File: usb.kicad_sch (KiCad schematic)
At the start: 69 parts, among them J13 USB-C_GCT_USB4105-GF-A, J3 USB-C_GCT_USB4105-GF-A, Q1 SSM3J332R, Q2 BC817-25W, Q3 BCM857BS-7-F, Q4 SSM3J332R, Q5 BCM857BS-7-F, U11 AP22652W6, U15 AP22652W6, U2 TPD4E05U06QDQARQ1, U4 AP62301_TSOT, U5 TPD4E05U06QDQARQ1, U8 AP62301_TSOT

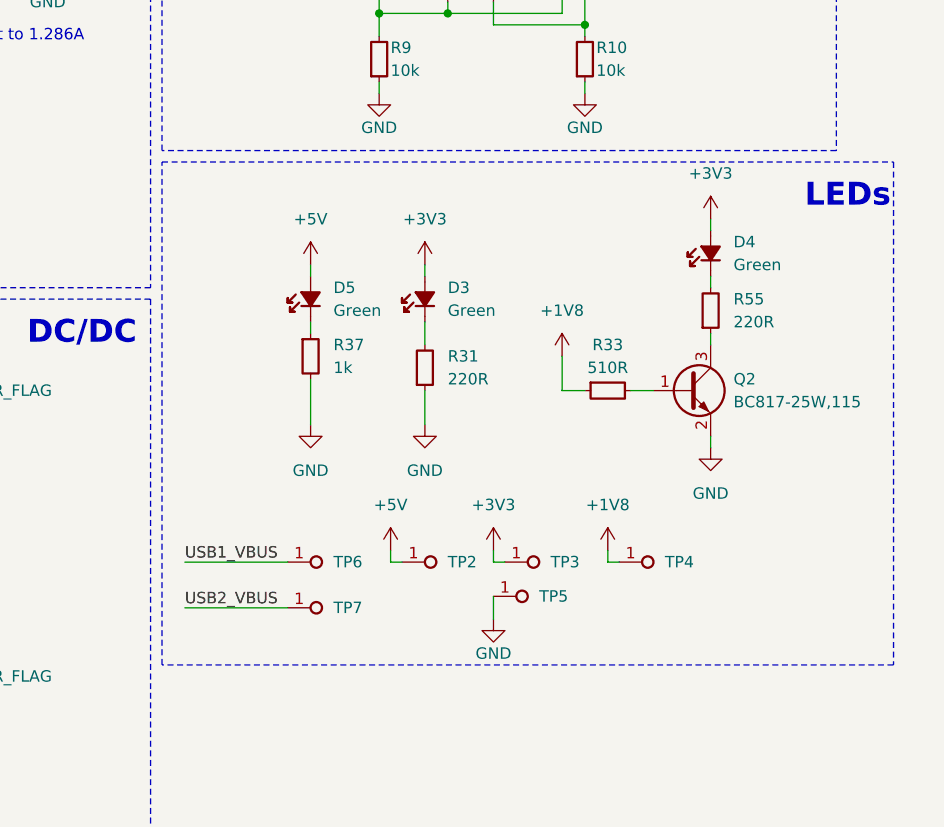
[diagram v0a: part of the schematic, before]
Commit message: [#71555] Change 1V8 status LED driver circuit
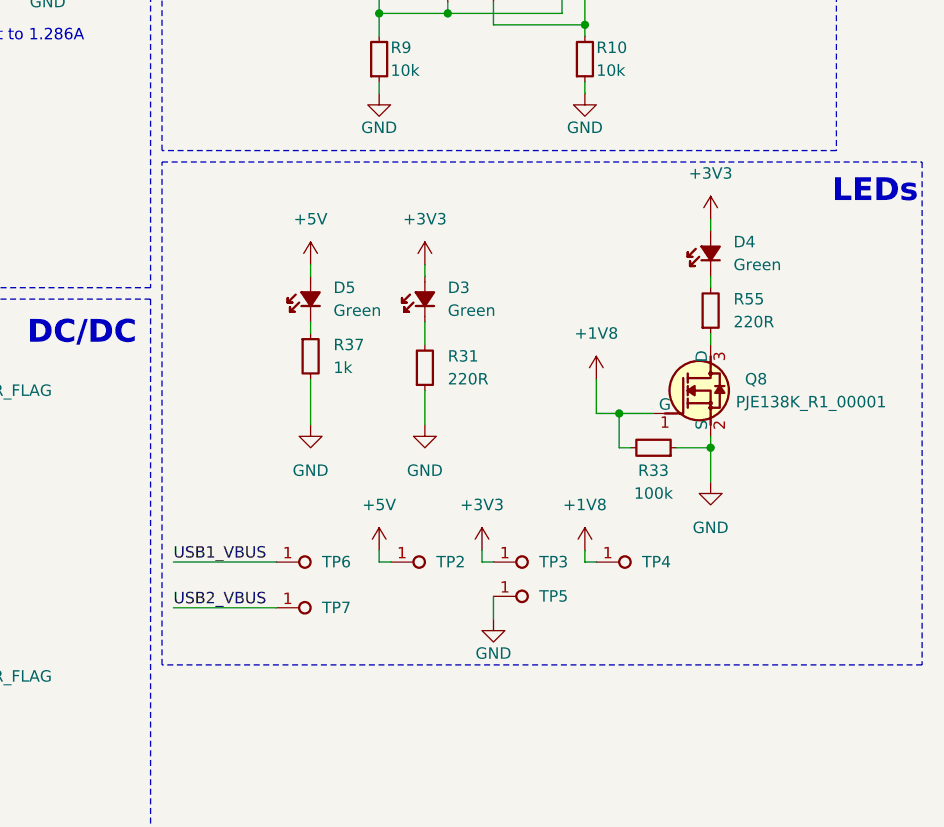
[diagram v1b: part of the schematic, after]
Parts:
- removed Q2: BC817-25W, antmicro-footprints:SOT-323, symbol antmicroTransistorsBipolarSingle:BC817-25W
- removed R33: R_510R_0402, antmicro-footprints:R_0402_1005Metric, symbol antmicroResistors0402:R_510R_0402
- added Q8: PJE138K, antmicro-footprints:SOT-523, symbol antmicroTransistorsFETsMOSFETsSingle:PJE138K
- added R33: R_100k_0402, antmicro-footprints:R_0402_1005Metric, symbol antmicroResistors0402:R_100k_0402
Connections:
- net +1V8: now also Q8.1 (G), R33.2
- net GND: now also Q8.2 (S), R33.1
- net at R55.1: now also Q8.3 (D)
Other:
- moved on the sheet: TP2, TP3, TP4, TP6, TP7

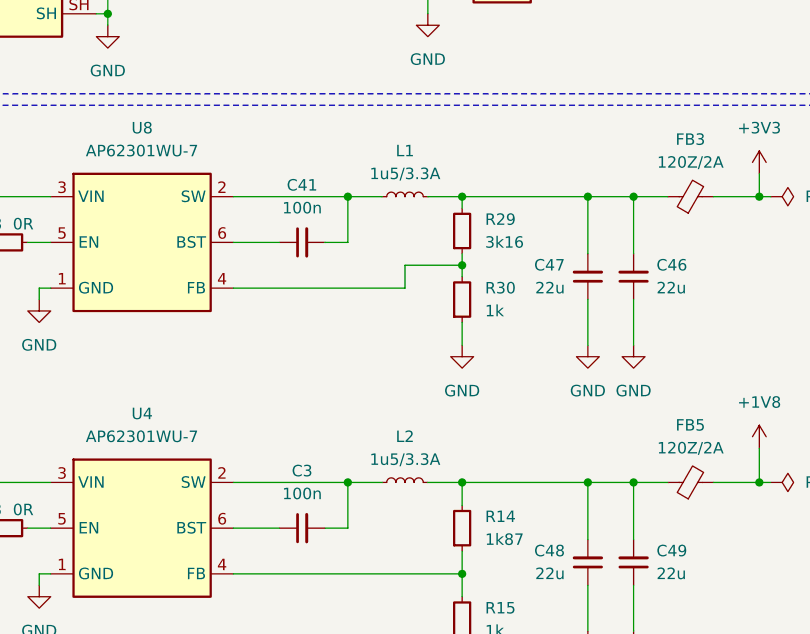
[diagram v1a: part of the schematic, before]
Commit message: [#71555] Change DCDC inductors to 2u2
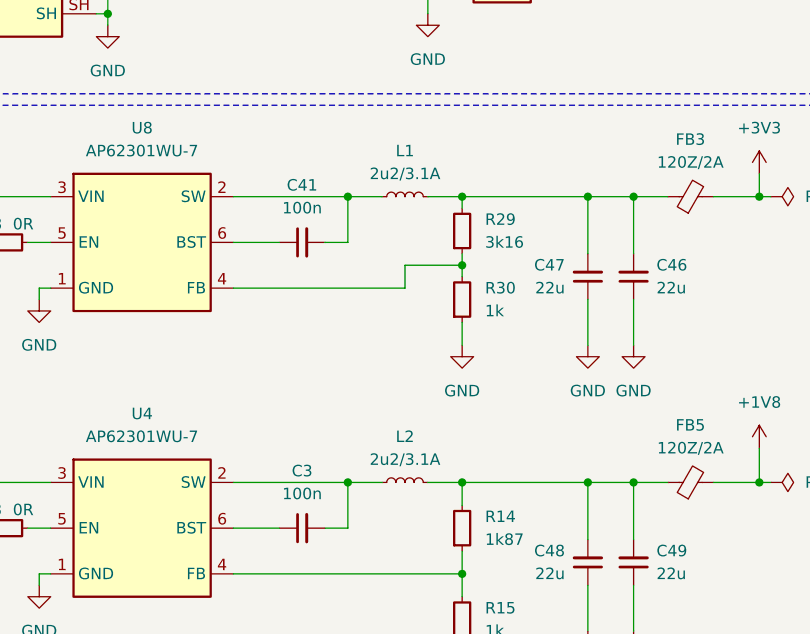
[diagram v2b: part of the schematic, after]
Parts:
- removed L1, L2: L_1u5_3.3A_1008, antmicro-footprints:L_1008_2520Metric, symbol antmicroFixedInductors:L_1u5_3.3A_1008
- added L1, L2: L_2u2_3.1A_Vishay-IFSC-1515AH-01, antmicro-footprints:L_Vishay-IFSC-1515AH, symbol antmicroFixedInductors:L_2u2_3.1A_Vishay-IFSC-1515AH-01
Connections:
- net at C3.2, U4.2 (SW): now also L2.1
- net at C46.2, C47.2, FB3.1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: now also L1.2
- net at C48.2, C49.2, FB5.1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: now also L2.2
- net at C41.2, U8.2 (SW): now also L1.1

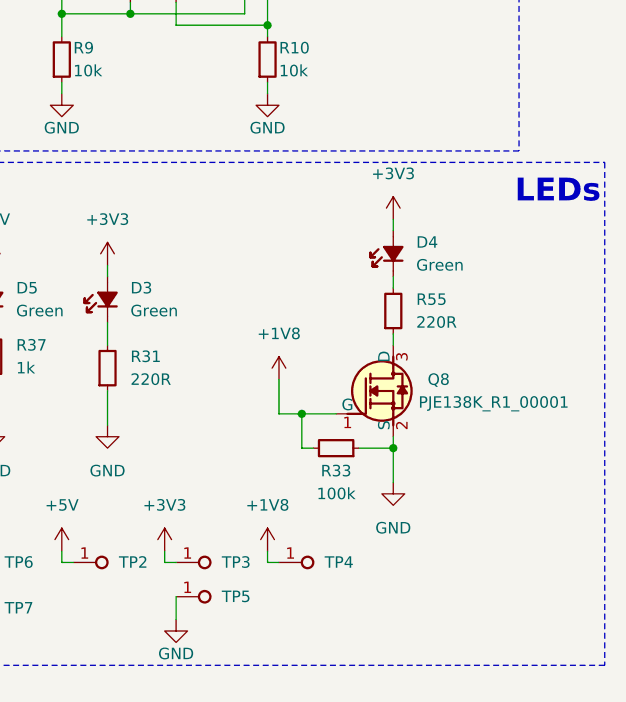
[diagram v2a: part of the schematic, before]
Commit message: [#71555] Switch LEDs switching transistors to BC817-25W
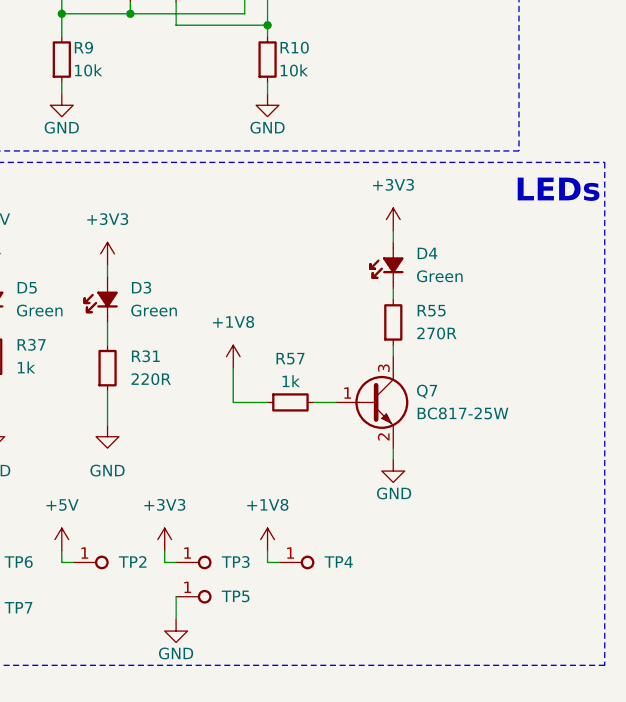
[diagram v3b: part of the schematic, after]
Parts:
- removed Q8: PJE138K, antmicro-footprints:SOT-523, symbol antmicroTransistorsFETsMOSFETsSingle:PJE138K
- removed R33: R_100k_0402, antmicro-footprints:R_0402_1005Metric, symbol antmicroResistors0402:R_100k_0402
- removed R55: R_220R_0402, antmicro-footprints:R_0402_1005Metric, symbol antmicroResistors0402:R_220R_0402
- added Q7: BC817-25W, antmicro-footprints:SOT-323, symbol antmicroTransistorsBipolarSingle:BC817-25W
- added R55: R_270R_0402, antmicro-footprints:R_0402_1005Metric, symbol antmicroResistors0402:R_270R_0402
- added R57: R_1k_0402, antmicro-footprints:R_0402_1005Metric, symbol antmicroResistors0402:R_1k_0402
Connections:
- net +1V8: now also R57.1
- net GND: now also Q7.2 (E)
- net at D4.1 (C): now also R55.2
- new net: Q7.1 (B), R57.2
- new net: Q7.3 (C), R55.1
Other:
- moved on the sheet: D4
